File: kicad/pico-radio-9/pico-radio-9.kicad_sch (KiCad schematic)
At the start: 45 parts, among them J1 HF Amplifier, J2 MW/SW antenna, J3 FM antenna, J4 SW antenna, J5 Batterry, Q1 PN2222A, Q2 PN2222A, Q3 PN2222A, SW1 Reset, U1 SI4732-A10-GS, U2 TFT_320x240, U3 KY-040, Y1 32.762kHz

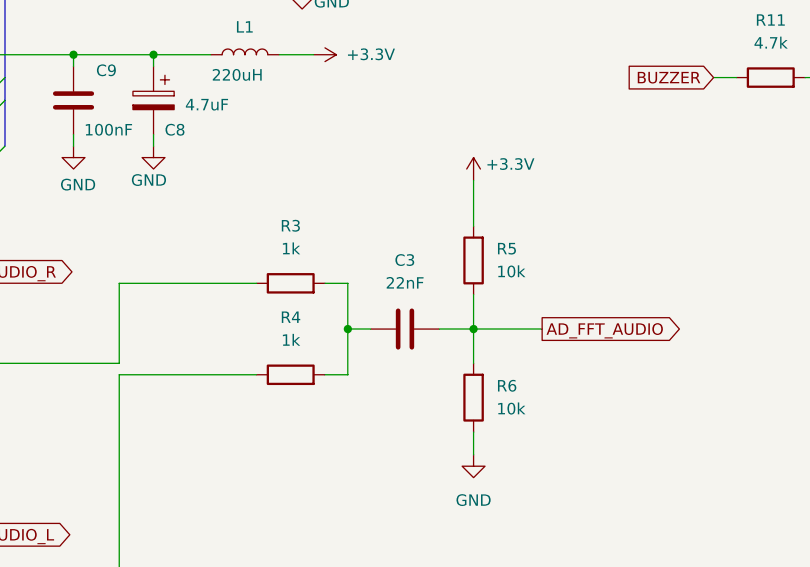
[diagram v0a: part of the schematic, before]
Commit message: HWSW mutestat + kicad file rename
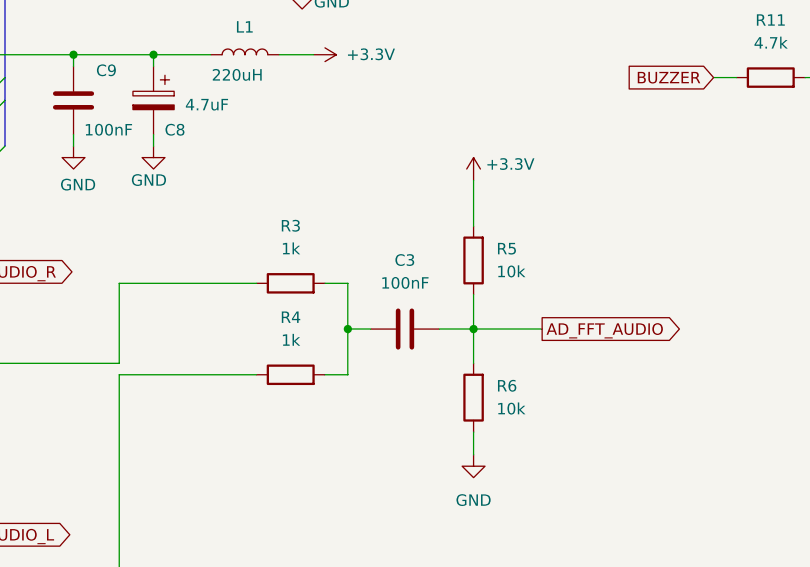
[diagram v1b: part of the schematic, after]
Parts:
- C3: value 22nF -> 100nF
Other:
- title: Pico radio-5 -> Pico radio-9
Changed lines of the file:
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@@
 	(paper "A4")
 	(title_block
-		(title "Pico radio-5")
+		(title "Pico radio-9")
 		(date "2025-08-04")
 	)
@@
 		)
 		(instances
-			(project "pico-radio-5"
+			(project "pico-radio-9"
 				(path "/b9640508-dcc6-4f6b-830f-c53a732dcb5b"
 					(reference "#PWR01")
@@
 		)
 		(instances
-			(project "pico-radio-5"
+			(project "pico-radio-9"
 				(path "/b9640508-dcc6-4f6b-830f-c53a732dcb5b"
 					(reference "#PWR032")
@@
 		)
 		(instances
-			(project "pico-radio-5"
+			(project "pico-radio-9"
 				(path "/b9640508-dcc6-4f6b-830f-c53a732dcb5b"
 					(reference "#PWR024")
@@
 		)
 		(instances
-			(project "pico-radio-5"
+			(project "pico-radio-9"
 				(path "/b9640508-dcc6-4f6b-830f-c53a732dcb5b"
 					(reference "#PWR027")
@@
 		)
 		(instances
-			(project "pico-radio-5"
+			(project "pico-radio-9"
 				(path "/b9640508-dcc6-4f6b-830f-c53a732dcb5b"
 					(reference "R6")
@@
 		)
 		(instances
-			(project "pico-radio-5"
+			(project "pico-radio-9"
 				(path "/b9640508-dcc6-4f6b-830f-c53a732dcb5b"
 					(reference "J4")
@@
 		)
 		(instances
-			(project "pico-radio-5"
+			(project "pico-radio-9"
 				(path "/b9640508-dcc6-4f6b-830f-c53a732dcb5b"
 					(reference "R10")
@@
 		)
 		(instances
-			(project "pico-radio-5"
+			(project "pico-radio-9"
 				(path "/b9640508-dcc6-4f6b-830f-c53a732dcb5b"
 					(reference "#PWR017")
@@
 		)
 		(instances
-			(project "pico-radio-5"
+			(project "pico-radio-9"
 				(path "/b9640508-dcc6-4f6b-830f-c53a732dcb5b"
 					(reference "C6")
@@
 		)
 		(instances
-			(project "pico-radio-5"
+			(project "pico-radio-9"
 				(path "/b9640508-dcc6-4f6b-830f-c53a732dcb5b"
 					(reference "#PWR020")
@@
 		)
 		(instances
-			(project "pico-radio-5"
+			(project "pico-radio-9"
 				(path "/b9640508-dcc6-4f6b-830f-c53a732dcb5b"
 					(reference "#PWR037")
@@
 		)
 		(instances
-			(project "pico-radio-5"
+			(project "pico-radio-9"
 				(path "/b9640508-dcc6-4f6b-830f-c53a732dcb5b"
 					(reference "R11")
@@
 		)
 		(instances
-			(project "pico-radio-5"
+			(project "pico-radio-9"
 				(path "/b9640508-dcc6-4f6b-830f-c53a732dcb5b"
 					(reference "#PWR036")
@@
 		)
 		(instances
-			(project "pico-radio-5"
+			(project "pico-radio-9"
 				(path "/b9640508-dcc6-4f6b-830f-c53a732dcb5b"
 					(reference "#PWR015")
@@
 		)
 		(instances
-			(project "pico-radio-5"
+			(project "pico-radio-9"
 				(path "/b9640508-dcc6-4f6b-830f-c53a732dcb5b"
 					(reference "R8")
@@
 		)
 		(instances
-			(project "pico-radio-5"
+			(project "pico-radio-9"
 				(path "/b9640508-dcc6-4f6b-830f-c53a732dcb5b"
 					(reference "#PWR025")
@@
 		)
 		(instances
-			(project "pico-radio-5"
+			(project "pico-radio-9"
 				(path "/b9640508-dcc6-4f6b-830f-c53a732dcb5b"
 					(reference "R5")
@@
 		)
 		(instances
-			(project "pico-radio-5"
+			(project "pico-radio-9"
 				(path "/b9640508-dcc6-4f6b-830f-c53a732dcb5b"
 					(reference "#PWR016")
@@
 		)
 		(instances
-			(project "pico-radio-5"
+			(project "pico-radio-9"
 				(path "/b9640508-dcc6-4f6b-830f-c53a732dcb5b"
 					(reference "#PWR029")
@@
 		)
 		(instances
-			(project "pico-radio-5"
+			(project "pico-radio-9"
 				(path "/b9640508-dcc6-4f6b-830f-c53a732dcb5b"
 					(reference "#PWR010")
@@
 		)
 		(instances
-			(project "pico-radio-5"
+			(project "pico-radio-9"
 				(path "/b9640508-dcc6-4f6b-830f-c53a732dcb5b"
 					(reference "R2")
@@
 		)
 		(instances
-			(project "pico-radio-5"
+			(project "pico-radio-9"
 				(path "/b9640508-dcc6-4f6b-830f-c53a732dcb5b"
 					(reference "R3")
@@
 		)
 		(instances
-			(project "pico-radio-5"
+			(project "pico-radio-9"
 				(path "/b9640508-dcc6-4f6b-830f-c53a732dcb5b"
 					(reference "Q2")
@@
 		)
 		(instances
-			(project "pico-radio-5"
+			(project "pico-radio-9"
 				(path "/b9640508-dcc6-4f6b-830f-c53a732dcb5b"
 					(reference "#PWR028")
@@
 		)
 		(instances
-			(project "pico-radio-5"
+			(project "pico-radio-9"
 				(path "/b9640508-dcc6-4f6b-830f-c53a732dcb5b"
 					(reference "C5")
@@
 		)
 		(instances
-			(project "pico-radio-5"
+			(project "pico-radio-9"
 				(path "/b9640508-dcc6-4f6b-830f-c53a732dcb5b"
 					(reference "C12")
@@
 		)
 		(instances
-			(project "pico-radio-5"
+			(project "pico-radio-9"
 				(path "/b9640508-dcc6-4f6b-830f-c53a732dcb5b"
 					(reference "C8")
@@
 		)
 		(instances
-			(project "pico-radio-5"
+			(project "pico-radio-9"
 				(path "/b9640508-dcc6-4f6b-830f-c53a732dcb5b"
 					(reference "C2")
@@
 		)
 		(instances
-			(project "pico-radio-5"
+			(project "pico-radio-9"
 				(path "/b9640508-dcc6-4f6b-830f-c53a732dcb5b"
 					(reference "C7")
@@
 		)
 		(instances
-			(project "pico-radio-5"
+			(project "pico-radio-9"
 				(path "/b9640508-dcc6-4f6b-830f-c53a732dcb5b"
 					(reference "#PWR035")
@@
 		)
 		(instances
-			(project "pico-radio-5"
+			(project "pico-radio-9"
 				(path "/b9640508-dcc6-4f6b-830f-c53a732dcb5b"
 					(reference "L2")
@@
 		)
 		(instances
-			(project "pico-radio-5"
+			(project "pico-radio-9"
 				(path "/b9640508-dcc6-4f6b-830f-c53a732dcb5b"
 					(reference "R7")
@@
 		)
 		(instances
-			(project "pico-radio-5"
+			(project "pico-radio-9"
 				(path "/b9640508-dcc6-4f6b-830f-c53a732dcb5b"
 					(reference "#PWR018")
@@
 		)
 		(instances
-			(project "pico-radio-5"
+			(project "pico-radio-9"
 				(path "/b9640508-dcc6-4f6b-830f-c53a732dcb5b"
 					(reference "#PWR040")
@@
 		)
 		(instances
-			(project "pico-radio-5"
+			(project "pico-radio-9"
 				(path "/b9640508-dcc6-4f6b-830f-c53a732dcb5b"
 					(reference "Q3")
@@
 		)
 		(instances
-			(project "pico-radio-5"
+			(project "pico-radio-9"
 				(path "/b9640508-dcc6-4f6b-830f-c53a732dcb5b"
 					(reference "#PWR019")
@@
 		)
 		(instances
-			(project "pico-radio-5"
+			(project "pico-radio-9"
 				(path "/b9640508-dcc6-4f6b-830f-c53a732dcb5b"
 					(reference "#PWR021")
@@
 		)
 		(instances
-			(project "pico-radio-5"
+			(project "pico-radio-9"
 				(path "/b9640508-dcc6-4f6b-830f-c53a732dcb5b"
 					(reference "#PWR023")
@@
 			)
 		)
-		(property "Value" "22nF"
+		(property "Value" "100nF"
 			(at 196.85 137.16 90)
 			(effects
@@
 		)
 		(instances
-			(project "pico-radio-5"
+			(project "pico-radio-9"
 				(path "/b9640508-dcc6-4f6b-830f-c53a732dcb5b"
 					(reference "#PWR034")
@@
 		)
 		(instances
-			(project "pico-radio-5"
+			(project "pico-radio-9"
 				(path "/b9640508-dcc6-4f6b-830f-c53a732dcb5b"
 					(reference "JP2")
@@
 		)
 		(instances
-			(project "pico-radio-5"
+			(project "pico-radio-9"
 				(path "/b9640508-dcc6-4f6b-830f-c53a732dcb5b"
 					(reference "#PWR014")
@@
 		)
 		(instances
-			(project "pico-radio-5"
+			(project "pico-radio-9"
 				(path "/b9640508-dcc6-4f6b-830f-c53a732dcb5b"
 					(reference "#PWR030")
@@
 		)
 		(instances
-			(project "pico-radio-5"
+			(project "pico-radio-9"
 				(path "/b9640508-dcc6-4f6b-830f-c53a732dcb5b"
 					(reference "#PWR026")
@@
 		)
 		(instances
-			(project "pico-radio-5"
+			(project "pico-radio-9"
 				(path "/b9640508-dcc6-4f6b-830f-c53a732dcb5b"
 					(reference "C10")
@@
 		)
 		(instances
-			(project "pico-radio-5"
+			(project "pico-radio-9"
 				(path "/b9640508-dcc6-4f6b-830f-c53a732dcb5b"
 					(reference "#PWR09")
@@
 		)
 		(instances
-			(project "pico-radio-5"
+			(project "pico-radio-9"
 				(path "/b9640508-dcc6-4f6b-830f-c53a732dcb5b"
 					(reference "#PWR022")
@@
 		)
 		(instances
-			(project "pico-radio-5"
+			(project "pico-radio-9"
 				(path "/b9640508-dcc6-4f6b-830f-c53a732dcb5b"
 					(reference "C11")
@@
 		)
 		(instances
-			(project "pico-radio-5"
+			(project "pico-radio-9"
 				(path "/b9640508-dcc6-4f6b-830f-c53a732dcb5b"
 					(reference "#PWR011")
@@
 		)
 		(instances
-			(project "pico-radio-5"
+			(project "pico-radio-9"
 				(path "/b9640508-dcc6-4f6b-830f-c53a732dcb5b"
 					(reference "C9")
@@
 		)
 		(instances
-			(project "pico-radio-5"
+			(project "pico-radio-9"
 				(path "/b9640508-dcc6-4f6b-830f-c53a732dcb5b"
 					(reference "#PWR039")
@@
 		)
 		(instances
-			(project "pico-radio-5"
+			(project "pico-radio-9"
 				(path "/b9640508-dcc6-4f6b-830f-c53a732dcb5b"
 					(reference "#PWR031")
@@
 		)
 		(instances
-			(project "pico-radio-5"
+			(project "pico-radio-9"
 				(path "/b9640508-dcc6-4f6b-830f-c53a732dcb5b"
 					(reference "R9")
@@
 		)
 		(instances
-			(project "pico-radio-5"
+			(project "pico-radio-9"
 				(path "/b9640508-dcc6-4f6b-830f-c53a732dcb5b"
 					(reference "L3")
@@
 		)
 		(instances
-			(project "pico-radio-5"
+			(project "pico-radio-9"
 				(path "/b9640508-dcc6-4f6b-830f-c53a732dcb5b"
 					(reference "R4")
@@
 		)
 		(instances
-			(project "pico-radio-5"
+			(project "pico-radio-9"
 				(path "/b9640508-dcc6-4f6b-830f-c53a732dcb5b"
 					(reference "#PWR033")

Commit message: Refactor code structure for improved readability and maintainability
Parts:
- C3: value 100nF -> 470nF
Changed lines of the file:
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@@
 			)
 		)
-		(property "Value" "100nF"
+		(property "Value" "470nF"
 			(at 196.85 137.16 90)
 			(effects

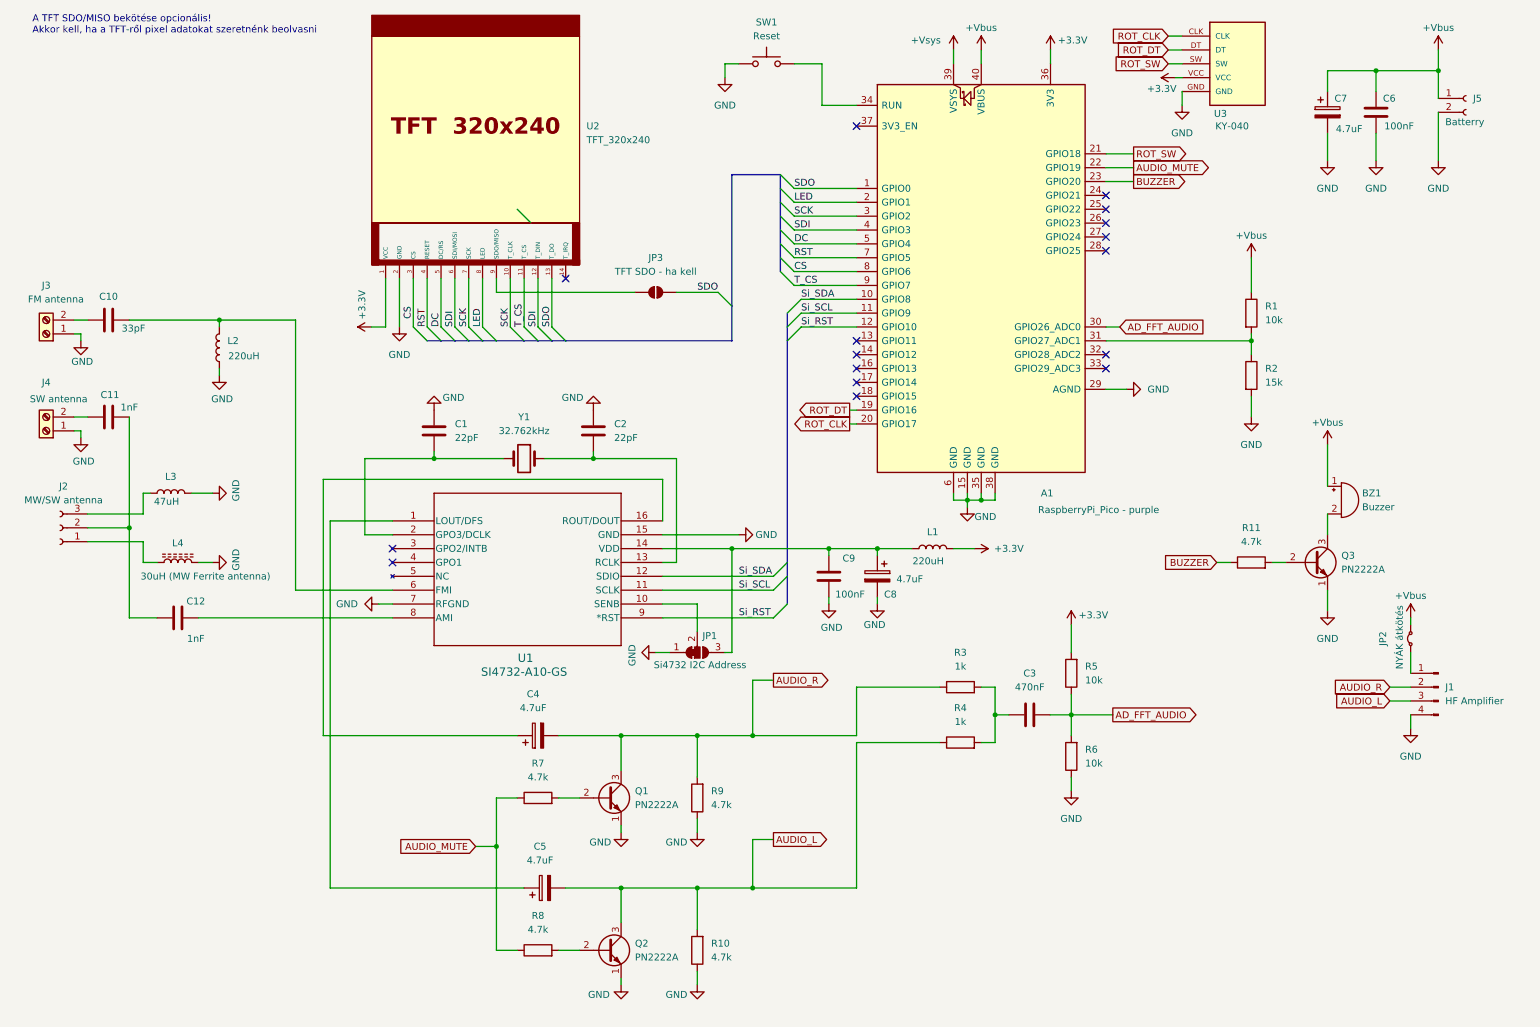
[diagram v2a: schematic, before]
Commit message: Add UICompTuningBar component for spectrum visualization
- Implemented UICompTuningBar class to display a tuning bar for frequency spectrum analysis.
- Added methods for updating spectrum data, drawing the tuning bar, and managing frequency markers.
- Integrated peak hold logic for better visualization of signal strength over time.
- Included color coding for bar heights based on magnitude.
- Optimized rendering with sprite support for improved performance.
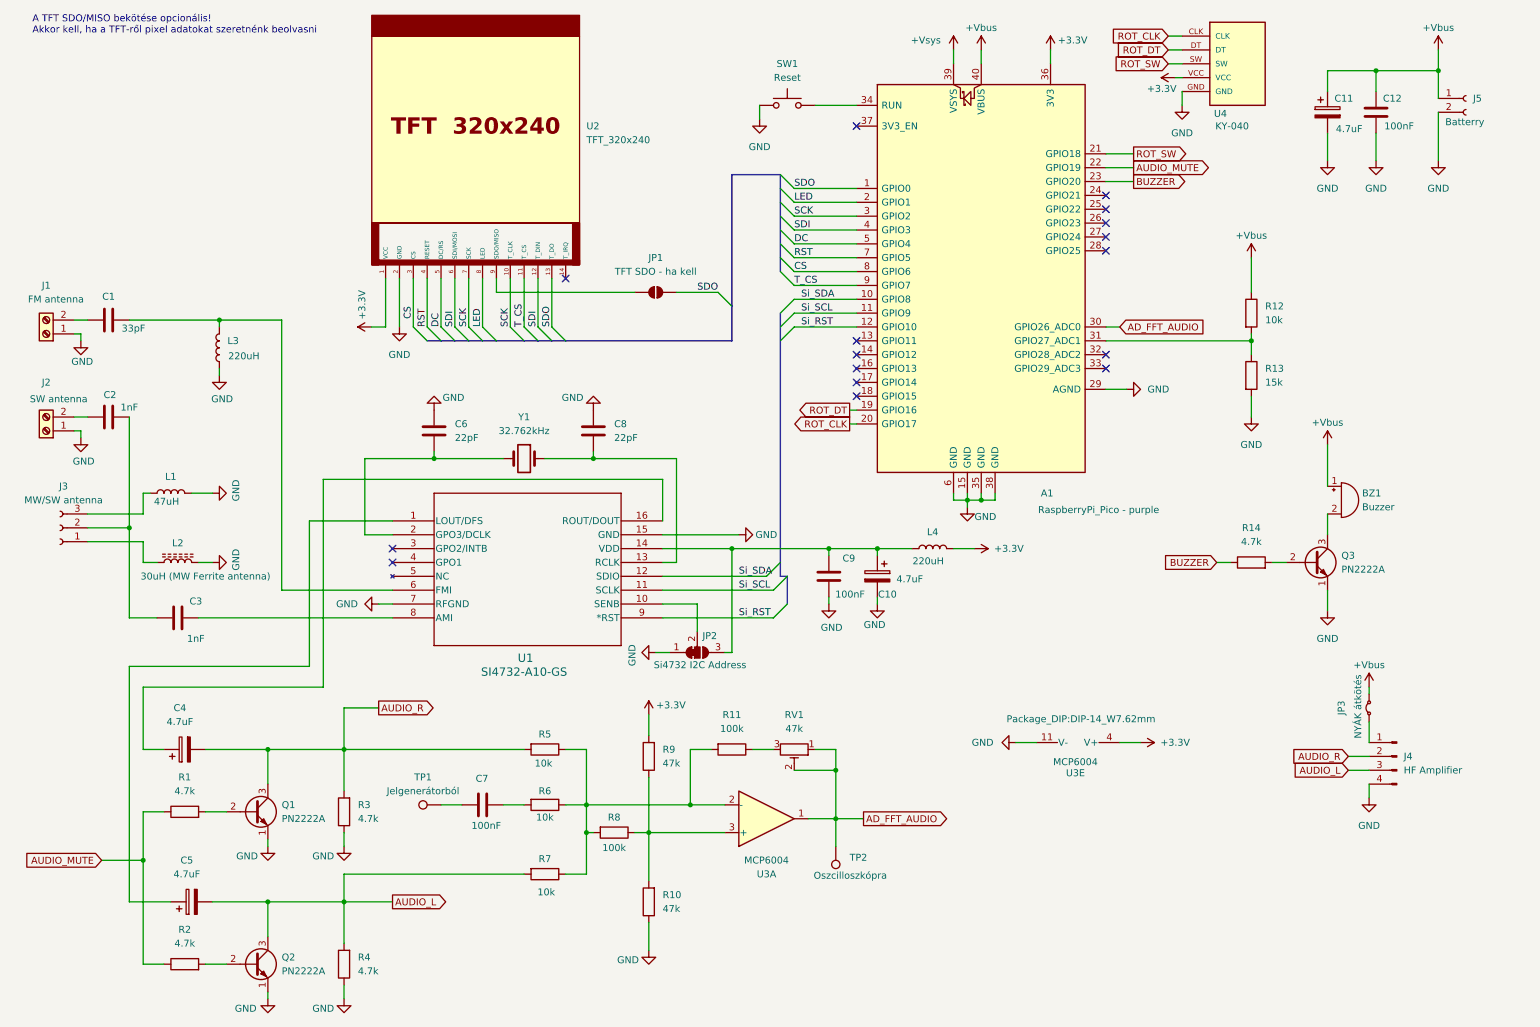
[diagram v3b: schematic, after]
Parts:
- removed C3: 470nF, Capacitor_THT:C_Disc_D7.0mm_W2.5mm_P5.00mm, symbol Device:C
- removed R3, R4: 1k, Resistor_THT:R_Axial_DIN0207_L6.3mm_D2.5mm_P10.16mm_Horizontal, symbol Device:R
- added C7: 100nF, Capacitor_THT:C_Disc_D7.0mm_W2.5mm_P5.00mm, symbol Device:C
- added R10, R9: 47k, Resistor_THT:R_Axial_DIN0207_L6.3mm_D2.5mm_P10.16mm_Horizontal, symbol Device:R
- added R11, R8: 100k, Resistor_THT:R_Axial_DIN0207_L6.3mm_D2.5mm_P10.16mm_Horizontal, symbol Device:R
- added R7: 10k, Resistor_THT:R_Axial_DIN0207_L6.3mm_D2.5mm_P10.16mm_Horizontal, symbol Device:R
- added RV1: 47k, Potentiometer_THT:Potentiometer_Runtron_RM-063_Horizontal, symbol Device:R_Potentiometer_Trim
- added TP1: Jelgenerátorból, TestPoint:TestPoint_Loop_D2.50mm_Drill1.0mm, symbol Connector:TestPoint
- added TP2: Oszcilloszkópra, TestPoint:TestPoint_Loop_D2.50mm_Drill1.0mm, symbol Connector:TestPoint
- added U3: MCP6004, Package_DIP:DIP-14_W7.62mm, symbol Amplifier_Operational:MCP6004
- renumbered C10 to C1, C8 to C10, C7 to C11, C6 to C12, C11 to C2, C12 to C3, C1 to C6, C2 to C8, J3 to J1, J4 to J2, J2 to J3, J1 to J4, JP3 to JP1, JP1 to JP2, JP2 to JP3, L3 to L1, L4 to L2, L2 to L3, L1 to L4, R7 to R1, R1 to R12, R2 to R13, R11 to R14, R8 to R2, R9 to R3, R10 to R4, U3 to U4
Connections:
- net +3.3V: now also R9.2, U3.4 (V+); no longer R5.2
- net AD_FFT_AUDIO: now also RV1.1, RV1.2, TP2.1, U3.1; no longer R5.1, R6.2
- net AUDIO_L: now also R7.2
- net AUDIO_R: now also R5.2
- net GND: now also R10.1, U3.11 (V-); no longer R6.1
- new net: R11.1, RV1.3
- new net: R11.2, R5.1, R6.1, R7.1, R8.2, U3.2 (-)
- new net: R10.2, R8.1, R9.1, U3.3 (+)
- new net: C7.1, R6.2
- new net: C7.2, TP1.1
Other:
- moved on the sheet: C4, C5, J4, JP3, Q1, Q2, R1, R2, R3, R4, SW1

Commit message: Refactor code structure for improved readability and maintainability
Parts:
- removed J5: Batterry, Connector_PinHeader_2.54mm:PinHeader_1x02_P2.54mm_Vertical, symbol Connector:Conn_01x02_Socket
- added J5: Batterry, Connector_PinHeader_2.54mm:PinHeader_1x03_P2.54mm_Vertical, symbol Connector:Conn_01x03_Socket
- added JP4, JP5: NYÁK átkötés, Resistor_THT:R_Axial_DIN0207_L6.3mm_D2.5mm_P10.16mm_Horizontal, symbol Jumper:Jumper_2_Small_Bridged
- Q1, Q2, Q3: footprint Package_TO_SOT_THT:TO-92_Inline -> Package_TO_SOT_THT:TO-92_Inline_Wide
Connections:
- net +Vbus: now also JP4.2 (B); no longer JP3.2 (B)
- net AD_FFT_AUDIO: now also U3.7; no longer U3.1
- net GND: now also J5.1 (Pin_1), J5.3 (Pin_3), JP5.1 (A), JP5.2 (B)
- net at R11.2, R5.1, R6.1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: now also U3.6 (-); no longer U3.2 (-)
- net at R10.2, R8.1, R9.1: now also U3.5 (+); no longer U3.3 (+)
- new net: J5.2 (Pin_2), JP3.2 (B), JP4.1 (A)
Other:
- moved on the sheet: BZ1, C11, C12, J4, JP3, Q3, R12, R13, R14

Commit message: Kicad PCB design
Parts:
- added H1, H2, H3, H4: MountingHole, MountingHole:MountingHole_3.2mm_M3, symbol Mechanical:MountingHole
- J3: value MW/SW antenna -> MW/SW antenna kapcsoló
- L2: value 30uH (MW Ferrite antenna) -> 30uH (MW Ferrit antenna)
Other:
- moved on the sheet: BZ1, C10, C11, C12, C9, JP5, L1, L2, L4, Q3, R14, U3E

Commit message: Vsys - Vbus power modification
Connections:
- net +Vsys: now also BZ1.1 (+), C11.1, C12.1, JP4.2 (B), R12.1
- removed net +Vbus: A1.40 (VBUS), BZ1.1 (+), C11.1, C12.1, JP4.2 (B), R12.1
- no-connect marks 16 -> 17
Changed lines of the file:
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@@
 	)
 	(no_connect
+		(at 187.96 22.86)
+	)
+	(no_connect
 		(at 210.82 54.61)
 	)
@@
 	(wire
 		(pts
-			(xy 187.96 20.32) (xy 187.96 22.86)
-		)
-		(stroke
-			(width 0)
-			(type default)
-		)
-	)
-	(wire
-		(pts
 			(xy 74.93 95.25) (xy 87.63 95.25)
 		)
@@
 			)
 		)
-		(property "Value" "+Vbus"
+		(property "Value" "+Vsys"
 			(at 232.41 54.356 0)
 			(effects
@@
 	)
 	(symbol
-		(lib_id "power:+BATT")
-		(at 187.96 20.32 0)
-		(unit 1)
-		(exclude_from_sim no)
-		(in_bom yes)
-		(on_board yes)
-		(dnp no)
-		(property "Reference" "#PWR025"
-			(at 187.96 24.13 0)
-			(effects
-				(font
-					(size 1.27 1.27)
-				)
-				(hide yes)
-			)
-		)
-		(property "Value" "+Vbus"
-			(at 187.96 16.256 0)
-			(effects
-				(font
-					(size 1.27 1.27)
-				)
-			)
-		)
-		(property "Footprint" ""
-			(at 187.96 20.32 0)
-			(effects
-				(font
-					(size 1.27 1.27)
-				)
-				(hide yes)
-			)
-		)
-		(property "Datasheet" ""
-			(at 187.96 20.32 0)
-			(effects
-				(font
-					(size 1.27 1.27)
-				)
-				(hide yes)
-			)
-		)
-		(property "Description" "Power symbol creates a global label with name \"+BATT\""
-			(at 187.96 20.32 0)
-			(effects
-				(font
-					(size 1.27 1.27)
-				)
-				(hide yes)
-			)
-		)
-		(pin "1"
-		)
-		(instances
-			(project ""
-				(path "/b9640508-dcc6-4f6b-830f-c53a732dcb5b"
-					(reference "#PWR025")
-					(unit 1)
-				)
-			)
-		)
-	)
-	(symbol
 		(lib_id "Device:R_Potentiometer_Trim")
 		(at 153.67 148.59 270)
@@
 			)
 		)
-		(property "Value" "+Vbus"
+		(property "Value" "+Vsys"
 			(at 266.7 32.766 0)
 			(effects
@@
 			)
 		)
-		(property "Value" "+Vbus"
+		(property "Value" "+Vsys"
 			(at 233.68 114.046 0)
 			(effects
